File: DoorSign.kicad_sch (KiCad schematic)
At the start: 38 parts, among them J1 Wall, J2 Taster, J3 Taster-LED, U1 Pico, U2 PC817, U3 LM2575-5.0BT

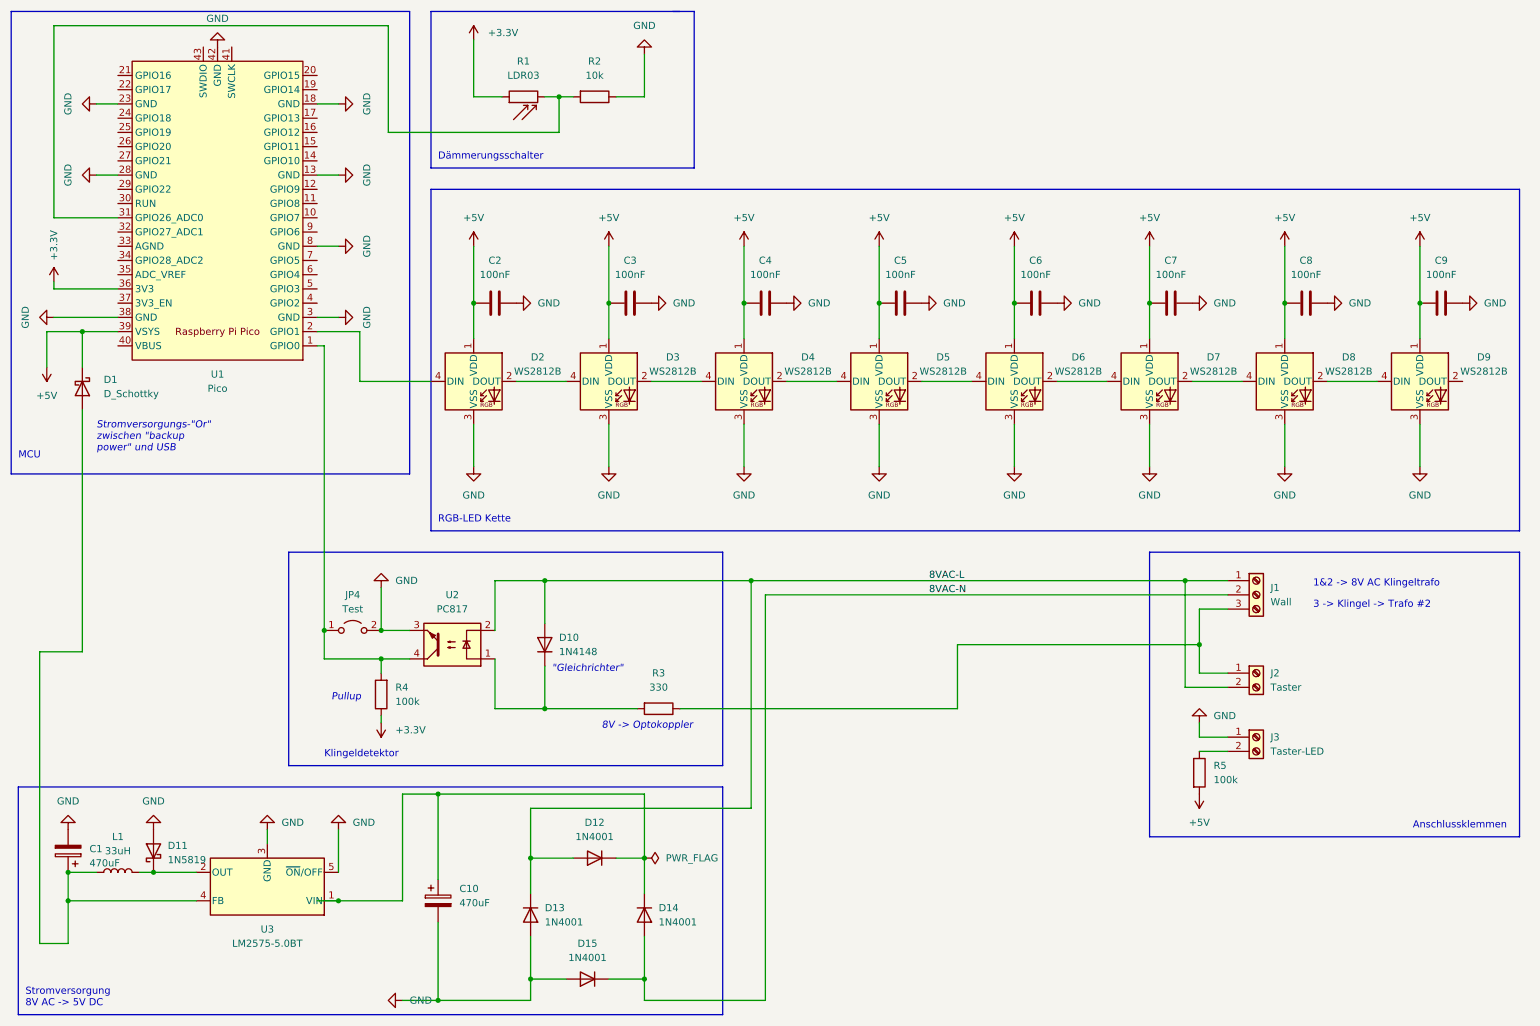
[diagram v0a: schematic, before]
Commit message: Rewired GPIOs for compatibility with Raspberry Pi Pico W
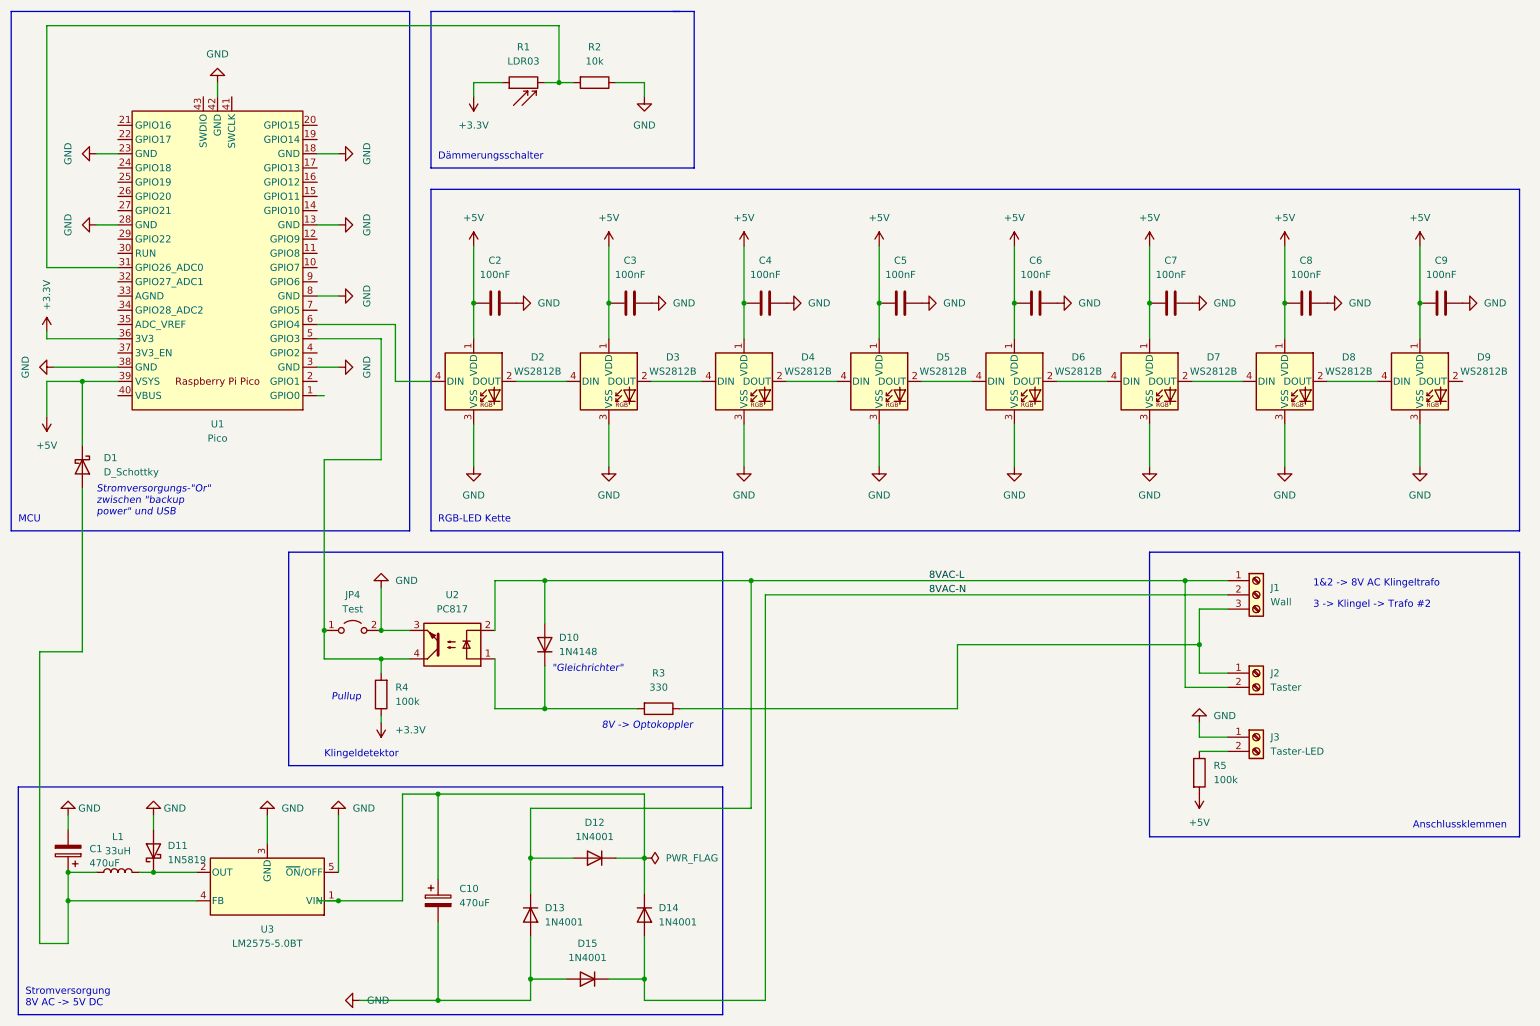
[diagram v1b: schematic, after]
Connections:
- net at JP4.1 (A), R4.2, U2.4: now also U1.5 (GPIO3); no longer U1.1 (GPIO0)
- net at D2.4 (DIN): now also U1.6 (GPIO4); no longer U1.2 (GPIO1)
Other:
- moved on the sheet: D1, R1, R2, U1

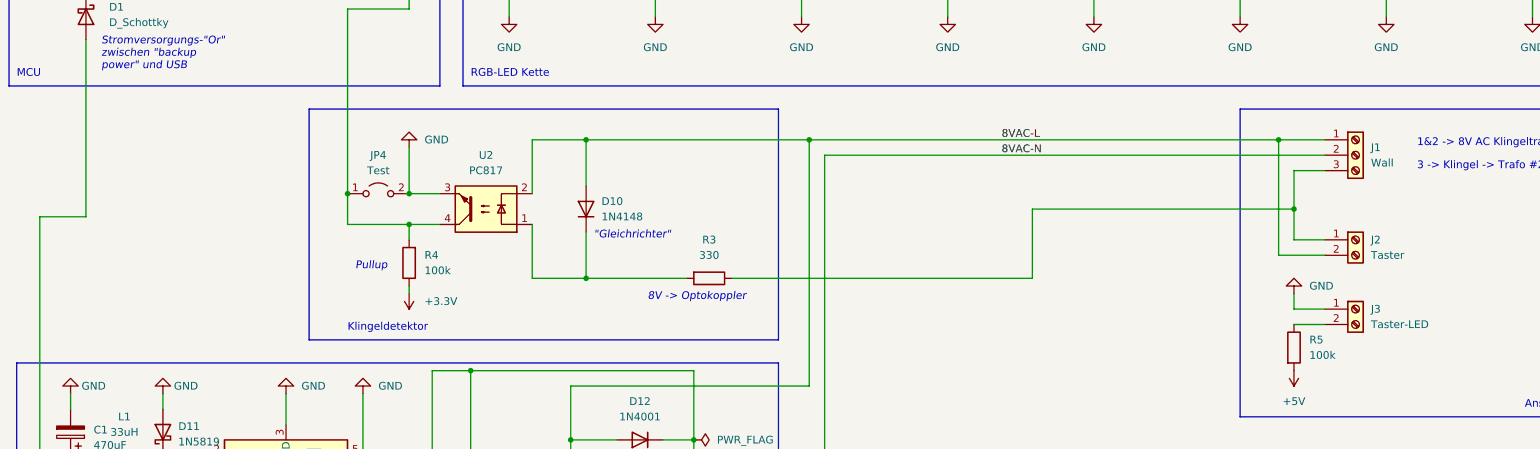
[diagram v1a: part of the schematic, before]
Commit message: Potential free contactor and pull-up/down added
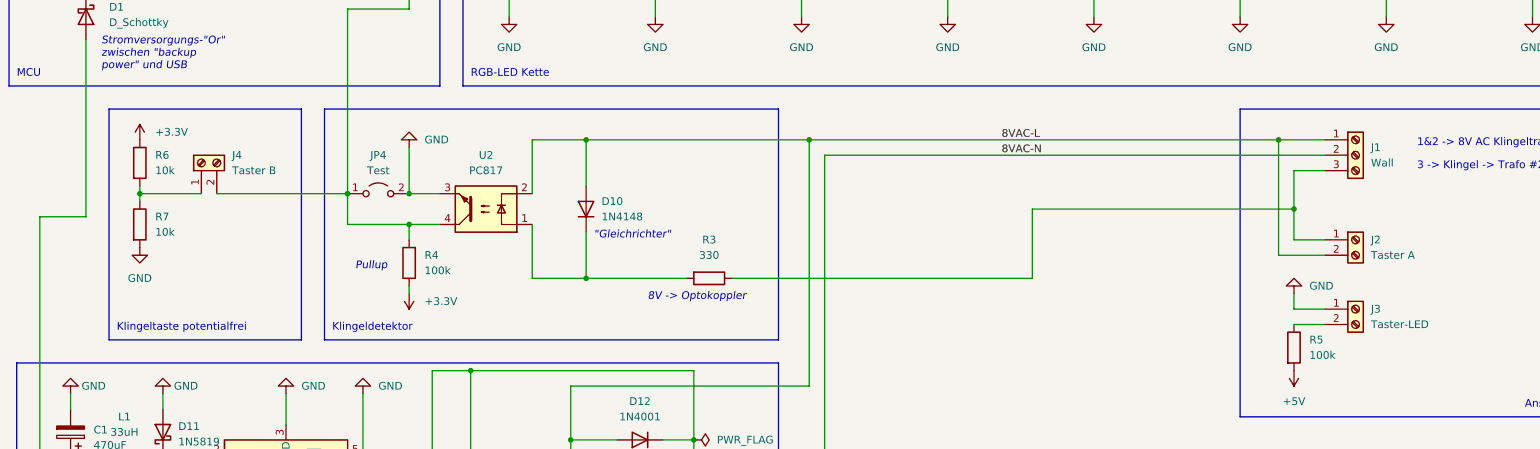
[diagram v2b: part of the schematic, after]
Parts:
- added J4: Taster B, TerminalBlock:TerminalBlock_Altech_AK300-2_P5.00mm, symbol Connector:Screw_Terminal_01x02
- added R6, R7: 10k, Resistor_THT:R_Axial_DIN0207_L6.3mm_D2.5mm_P15.24mm_Horizontal, symbol Device:R
- J2: value Taster -> Taster A
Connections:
- net +3.3V: now also R6.1
- net GND: now also R7.2
- net at JP4.1 (A), R4.2, U1.5 (GPIO3)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: now also J4.2 (Pin_2)
- new net: J4.1 (Pin_1), R6.2, R7.1
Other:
- note added: "Klingeltaste potentialfrei"
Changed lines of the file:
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@@
     (title "Türschild Heinrichsweg 9, 52249 Eschweiler")
   )
+  (junction (at 35.56 127) (diameter 0) (color 0 0 0 0)
+  )
   (junction (at 39.37 170.18) (diameter 0) (color 0 0 0 0)
   )
@@
     (stroke (width 0) (type default) (color 0 0 0 0))
   )
+  (wire (pts (xy 35.56 127) (xy 45.72 127))
+    (stroke (width 0) (type default) (color 0 0 0 0))
+  )
   (wire (pts (xy 20.32 19.05) (xy 20.32 62.23))
     (stroke (width 0) (type default) (color 0 0 0 0))
@@
     (stroke (width 0) (type default) (color 0 0 0 0))
   )
-  (polyline (pts (xy 140.97 151.13) (xy 63.5 151.13))
+  (polyline (pts (xy 140.97 151.13) (xy 66.04 151.13))
     (stroke (width 0) (type default) (color 0 0 0 0))
   )
@@
     (stroke (width 0) (type default) (color 0 0 0 0))
   )
-  (polyline (pts (xy 63.5 113.03) (xy 140.97 113.03))
+  (polyline (pts (xy 66.04 113.03) (xy 140.97 113.03))
     (stroke (width 0) (type default) (color 0 0 0 0))
   )
@@
     (stroke (width 0) (type default) (color 0 0 0 0))
   )
-  (polyline (pts (xy 63.5 151.13) (xy 63.5 113.03))
+  (polyline (pts (xy 66.04 151.13) (xy 66.04 113.03))
     (stroke (width 0) (type default) (color 0 0 0 0))
   )
@@
     (stroke (width 0) (type default) (color 0 0 0 0))
   )
+  (polyline (pts (xy 62.23 113.03) (xy 62.23 151.13))
+    (stroke (width 0) (type default) (color 0 0 0 0))
+  )
   (wire (pts (xy 146.05 118.11) (xy 146.05 158.75))
     (stroke (width 0) (type default) (color 0 0 0 0))
@@
     (stroke (width 0) (type default) (color 0 0 0 0))
   )
+  (wire (pts (xy 35.56 125.73) (xy 35.56 127))
+    (stroke (width 0) (type default) (color 0 0 0 0))
+  )
   (wire (pts (xy 226.06 123.19) (xy 226.06 129.54))
     (stroke (width 0) (type default) (color 0 0 0 0))
@@
     (stroke (width 0) (type default) (color 0 0 0 0))
   )
+  (wire (pts (xy 48.26 127) (xy 69.85 127))
+    (stroke (width 0) (type default) (color 0 0 0 0))
+  )
   (wire (pts (xy 127 167.64) (xy 127 156.21))
     (stroke (width 0) (type default) (color 0 0 0 0))
@@
     (stroke (width 0) (type default) (color 0 0 0 0))
   )
+  (polyline (pts (xy 30.48 151.13) (xy 30.48 113.03))
+    (stroke (width 0) (type default) (color 0 0 0 0))
+  )
   (wire (pts (xy 96.52 29.21) (xy 96.52 31.75))
     (stroke (width 0) (type default) (color 0 0 0 0))
@@
     (stroke (width 0) (type default) (color 0 0 0 0))
   )
+  (polyline (pts (xy 62.23 151.13) (xy 30.48 151.13))
+    (stroke (width 0) (type default) (color 0 0 0 0))
+  )
   (wire (pts (xy 120.65 189.23) (xy 127 189.23))
     (stroke (width 0) (type default) (color 0 0 0 0))
@@
     (stroke (width 0) (type default) (color 0 0 0 0))
   )
+  (polyline (pts (xy 30.48 113.03) (xy 62.23 113.03))
+    (stroke (width 0) (type default) (color 0 0 0 0))
+  )
   (wire (pts (xy 72.39 160.02) (xy 72.39 170.18))
     (stroke (width 0) (type default) (color 0 0 0 0))
@@
     (stroke (width 0) (type default) (color 0 0 0 0))
   )
+  (wire (pts (xy 35.56 127) (xy 35.56 128.27))
+    (stroke (width 0) (type default) (color 0 0 0 0))
+  )
   (wire (pts (xy 127 193.04) (xy 148.59 193.04))
     (stroke (width 0) (type default) (color 0 0 0 0))
@@
   (wire (pts (xy 20.32 62.23) (xy 33.02 62.23))
     (stroke (width 0) (type default) (color 0 0 0 0))
+  )
+  (text "Klingeltaste potentialfrei" (at 31.75 149.86 0)
+    (effects (font (size 1.27 1.27)) (justify left bottom))
   )
   (text "RGB-LED Kette" (at 90.17 107.95 0)
@@
     (effects (font (size 1.27 1.27) italic) (justify left bottom))
   )
-  (text "Klingeldetektor" (at 69.85 149.86 0)
+  (text "Klingeldetektor" (at 67.31 149.86 0)
     (effects (font (size 1.27 1.27)) (justify left bottom))
   )
@@
     (pin "2")
   )
+  (symbol (lib_id "Connector:Screw_Terminal_01x02") (at 45.72 121.92 90) (unit 1)
+    (in_bom yes) (on_board yes) (fields_autoplaced)
+    (property "Reference" "J4" (id 0) (at 50.8 120.6499 90)
+      (effects (font (size 1.27 1.27)) (justify right))
+    )
+    (property "Value" "Taster B" (id 1) (at 50.8 123.1899 90)
+      (effects (font (size 1.27 1.27)) (justify right))
+    )
+    (property "Footprint" "TerminalBlock:TerminalBlock_Altech_AK300-2_P5.00mm" (id 2) (at 45.72 121.92 0)
+      (effects (font (size 1.27 1.27)) hide)
+    )
+    (property "Datasheet" "~" (id 3) (at 45.72 121.92 0)
+      (effects (font (size 1.27 1.27)) hide)
+    )
+    (pin "1")
+    (pin "2")
+  )
   (symbol (lib_id "power:+3.3V") (at 80.01 143.51 180) (unit 1)
     (in_bom yes) (on_board yes) (fields_autoplaced)
@@
       (effects (font (size 1.27 1.27)) (justify left))
     )
-    (property "Value" "Taster" (id 1) (at 238.76 137.1599 0)
+    (property "Value" "Taster A" (id 1) (at 238.76 137.1599 0)
       (effects (font (size 1.27 1.27)) (justify left))
     )
@@
     )
     (property "Datasheet" "~" (id 3) (at 24.13 166.37 0)
+      (effects (font (size 1.27 1.27)) hide)
+    )
+    (pin "1")
+    (pin "2")
+  )
+  (symbol (lib_id "Device:R") (at 35.56 132.08 0) (unit 1)
+    (in_bom yes) (on_board yes) (fields_autoplaced)
+    (property "Reference" "R7" (id 0) (at 38.1 130.8099 0)
+      (effects (font (size 1.27 1.27)) (justify left))
+    )
+    (property "Value" "10k" (id 1) (at 38.1 133.3499 0)
+      (effects (font (size 1.27 1.27)) (justify left))
+    )
+    (property "Footprint" "Resistor_THT:R_Axial_DIN0207_L6.3mm_D2.5mm_P15.24mm_Horizontal" (id 2) (at 33.782 132.08 90)
+      (effects (font (size 1.27 1.27)) hide)
+    )
+    (property "Datasheet" "~" (id 3) (at 35.56 132.08 0)
       (effects (font (size 1.27 1.27)) hide)
     )
@@
     (pin "1")
   )
+  (symbol (lib_id "power:GND") (at 35.56 135.89 0) (unit 1)
+    (in_bom yes) (on_board yes)
+    (property "Reference" "#PWR0113" (id 0) (at 35.56 142.24 0)
+      (effects (font (size 1.27 1.27)) hide)
+    )
+    (property "Value" "GND" (id 1) (at 35.56 140.97 0))
+    (property "Footprint" "" (id 2) (at 35.56 135.89 0)
+      (effects (font (size 1.27 1.27)) hide)
+    )
+    (property "Datasheet" "" (id 3) (at 35.56 135.89 0)
+      (effects (font (size 1.27 1.27)) hide)
+    )
+    (pin "1")
+  )
   (symbol (lib_id "power:GND") (at 50.8 29.21 180) (unit 1)
     (in_bom yes) (on_board yes)
@@
     )
     (property "Datasheet" "http://www.vishay.com/docs/88503/1n4001.pdf" (id 3) (at 116.84 189.23 0)
+      (effects (font (size 1.27 1.27)) hide)
+    )
+    (pin "1")
+    (pin "2")
+  )
+  (symbol (lib_id "Device:R") (at 35.56 121.92 0) (unit 1)
+    (in_bom yes) (on_board yes) (fields_autoplaced)
+    (property "Reference" "R6" (id 0) (at 38.1 120.6499 0)
+      (effects (font (size 1.27 1.27)) (justify left))
+    )
+    (property "Value" "10k" (id 1) (at 38.1 123.1899 0)
+      (effects (font (size 1.27 1.27)) (justify left))
+    )
+    (property "Footprint" "Resistor_THT:R_Axial_DIN0207_L6.3mm_D2.5mm_P15.24mm_Horizontal" (id 2) (at 33.782 121.92 90)
+      (effects (font (size 1.27 1.27)) hide)
+    )
+    (property "Datasheet" "~" (id 3) (at 35.56 121.92 0)
       (effects (font (size 1.27 1.27)) hide)
     )
@@
     )
     (property "Datasheet" "" (id 3) (at 59.69 160.02 0)
+      (effects (font (size 1.27 1.27)) hide)
+    )
+    (pin "1")
+  )
+  (symbol (lib_id "power:+3.3V") (at 35.56 118.11 0) (unit 1)
+    (in_bom yes) (on_board yes) (fields_autoplaced)
+    (property "Reference" "#PWR0114" (id 0) (at 35.56 121.92 0)
+      (effects (font (size 1.27 1.27)) hide)
+    )
+    (property "Value" "+3.3V" (id 1) (at 38.1 116.8399 0)
+      (effects (font (size 1.27 1.27)) (justify left))
+    )
+    (property "Footprint" "" (id 2) (at 35.56 118.11 0)
+      (effects (font (size 1.27 1.27)) hide)
+    )
+    (property "Datasheet" "" (id 3) (at 35.56 118.11 0)
       (effects (font (size 1.27 1.27)) hide)
     )
@@
       (reference "#PWR0112") (unit 1) (value "GND") (footprint "")
     )
+    (path "/6dbd6a04-3371-42e4-be2a-6fda8080c888"
+      (reference "#PWR0113") (unit 1) (value "GND") (footprint "")
+    )
+    (path "/9f0410f5-5695-45d0-bf15-9df337547603"
+      (reference "#PWR0114") (unit 1) (value "+3.3V") (footprint "")
+    )
     (path "/49927729-dc2e-4ac4-b7aa-0e4f2f15cd80"
       (reference "C1") (unit 1) (value "470uF") (footprint "Capacitor_THT:CP_Radial_D12.5mm_P5.00mm")
@@
     )
     (path "/4009cc8e-aa7e-40e9-9904-068998d70662"
-      (reference "J2") (unit 1) (value "Taster") (footprint "TerminalBlock:TerminalBlock_Altech_AK300-2_P5.00mm")
+      (reference "J2") (unit 1) (value "Taster A") (footprint "TerminalBlock:TerminalBlock_Altech_AK300-2_P5.00mm")
     )
     (path "/583b5251-ba56-4628-abf6-bab842882868"
       (reference "J3") (unit 1) (value "Taster-LED") (footprint "TerminalBlock:TerminalBlock_Altech_AK300-2_P5.00mm")
     )
+    (path "/3c2186f3-36c7-4c1f-8754-f4f1cbfb7106"
+      (reference "J4") (unit 1) (value "Taster B") (footprint "TerminalBlock:TerminalBlock_Altech_AK300-2_P5.00mm")
+    )
     (path "/20276cc4-2770-42c9-b574-b05a75aa9cd5"
       (reference "JP4") (unit 1) (value "Test") (footprint "TestPoint:TestPoint_2Pads_Pitch2.54mm_Drill0.8mm")
@@
       (reference "R5") (unit 1) (value "100k") (footprint "Resistor_THT:R_Axial_DIN0207_L6.3mm_D2.5mm_P15.24mm_Horizontal")
     )
+    (path "/71231839-0498-481c-8db3-6f042260f8dd"
+      (reference "R6") (unit 1) (value "10k") (footprint "Resistor_THT:R_Axial_DIN0207_L6.3mm_D2.5mm_P15.24mm_Horizontal")
+    )
+    (path "/4b43555d-9753-4553-a51e-5175119fbfc0"
+      (reference "R7") (unit 1) (value "10k") (footprint "Resistor_THT:R_Axial_DIN0207_L6.3mm_D2.5mm_P15.24mm_Horizontal")
+    )
     (path "/f3d4ba1e-1075-4b33-baff-3d0396fc3cd4"
